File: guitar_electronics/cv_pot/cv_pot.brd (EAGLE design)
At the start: 17 x 24 mm, 8 parts

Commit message: push Nexus peripheral files
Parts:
- removed R1: 20K, resistor:R0402
- removed SJ1: (no value), jumper:SJ
- added C3: 1uF, resistor:C0603
- added U1: L78LXX, CYCFI_Power:SOT89
- C1: device resistor:C0603 -> resistor:C0402
- C2: device resistor:C0805 -> resistor:C0603
- moved C1 10.9 mm to (12.0, 8.00), turned to 180 degrees
- moved C2 5.62 mm to (12.0, 19.0), turned to 0 degrees
- moved H1 3.00 mm to (5.50, 19.0)
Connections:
- net GND: now also C2.1, C3.1, U1.2, U1.2@1; no longer C2.2
- net N$1: now also C2.2, U1.3; no longer C2.1, R1.2, SJ1.2
- net N$2: now also C3.2, U1.1; no longer R1.1, SJ1.1
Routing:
- net GND: track 64.9 -> 0.00 mm, vias 3 -> 0
- net N$1: track 21.1 -> 5.76 mm, vias 2 -> 0
- net N$2: track 22.9 -> 15.1 mm
- net OUT: track 26.8 -> 26.2 mm
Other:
- board text added: "CV POT v2.5"
- board text added: "GND"
- board text added: "V+"
- board text removed: "+"
- board text removed: "-"
- board text removed: "C1"
- board text removed: "CV POT"
- board text removed: "R1"

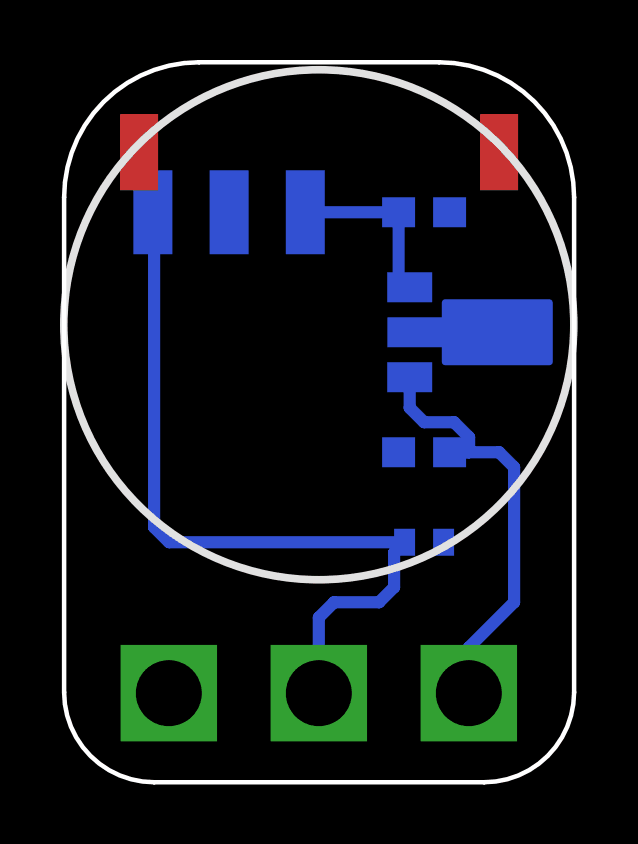
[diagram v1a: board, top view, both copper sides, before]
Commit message: updated schematic and bom files for cv pot
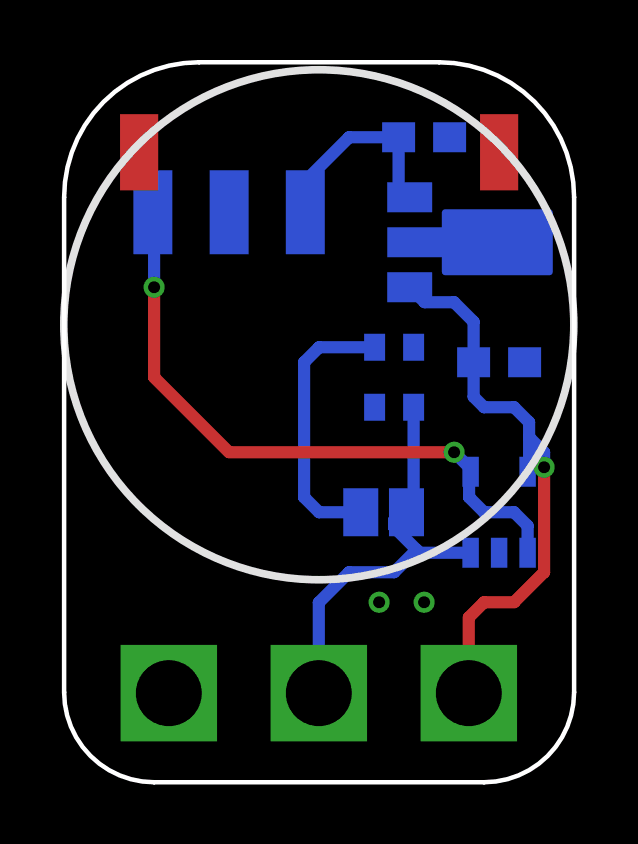
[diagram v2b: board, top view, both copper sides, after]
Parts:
- added R1: (no value), rcl:R0402
- added SJ1: (no value), jumper:SJ
- added U2: TLV6001, CYCFI_semicon:SOT23-5
- moved C1 4.61 mm to (11.0, 12.5), turned to 0 degrees
- moved C3 3.91 mm to (14.5, 14.0), turned to 0 degrees
- moved U1 3.00 mm to (13.5, 18.0)
- moved C2 2.50 mm to (12.0, 21.5)
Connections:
- removed net OUT: C1.1, H1.P$1, POT1.A2
- new net N$3: C1.1, POT1.A2, SJ1.2, U2.3
- new net N$4: R1.2, SJ1.1
- new net N$5: H1.P$1, U2.1, U2.4
- net GND: now also R1.1, U2.2
- net N$2: now also U2.5
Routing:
- net OUT: track 26.2 -> 0.00 mm
- net N$5: track 0.00 -> 21.5 mm, vias 0 -> 2
- net N$3: track 0.00 -> 14.2 mm
- net N$4: track 0.00 -> 9.15 mm
- net N$2: track 15.1 -> 19.3 mm, vias 0 -> 1
- net N$1: track 5.76 -> 6.91 mm
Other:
- board text added: "CV POT v2.6"
- board text removed: "CV POT v2.5"
